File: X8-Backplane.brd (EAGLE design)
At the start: 122.1 x 106.6 mm, 18 parts, among them U1 BD6221FSOP, U2 MIC29501-5.0WU, U3 MIC29501-5.0WU, U4 FQB27P06, U5 FQB27P06, U6 FQB27P06

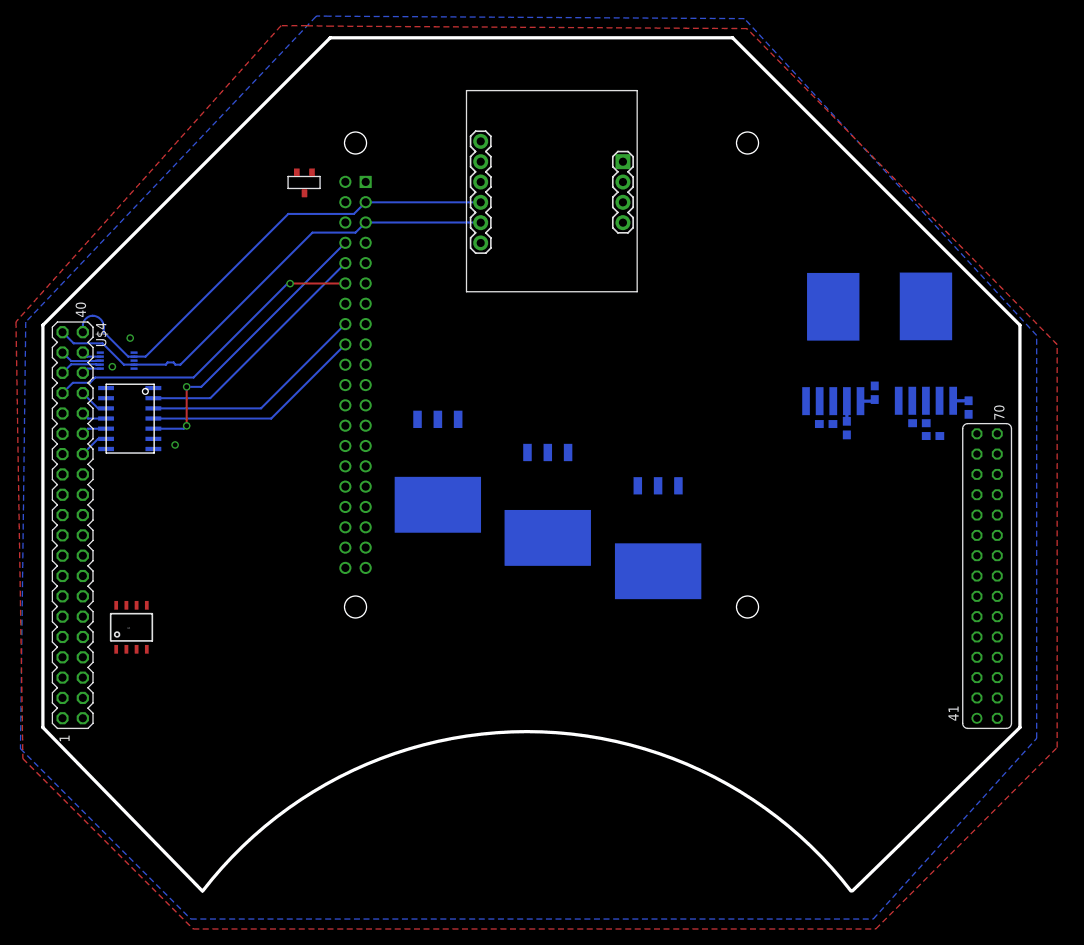
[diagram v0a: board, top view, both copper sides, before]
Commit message: Almost done with routing - stil have to add vias and extra debugging pinouts
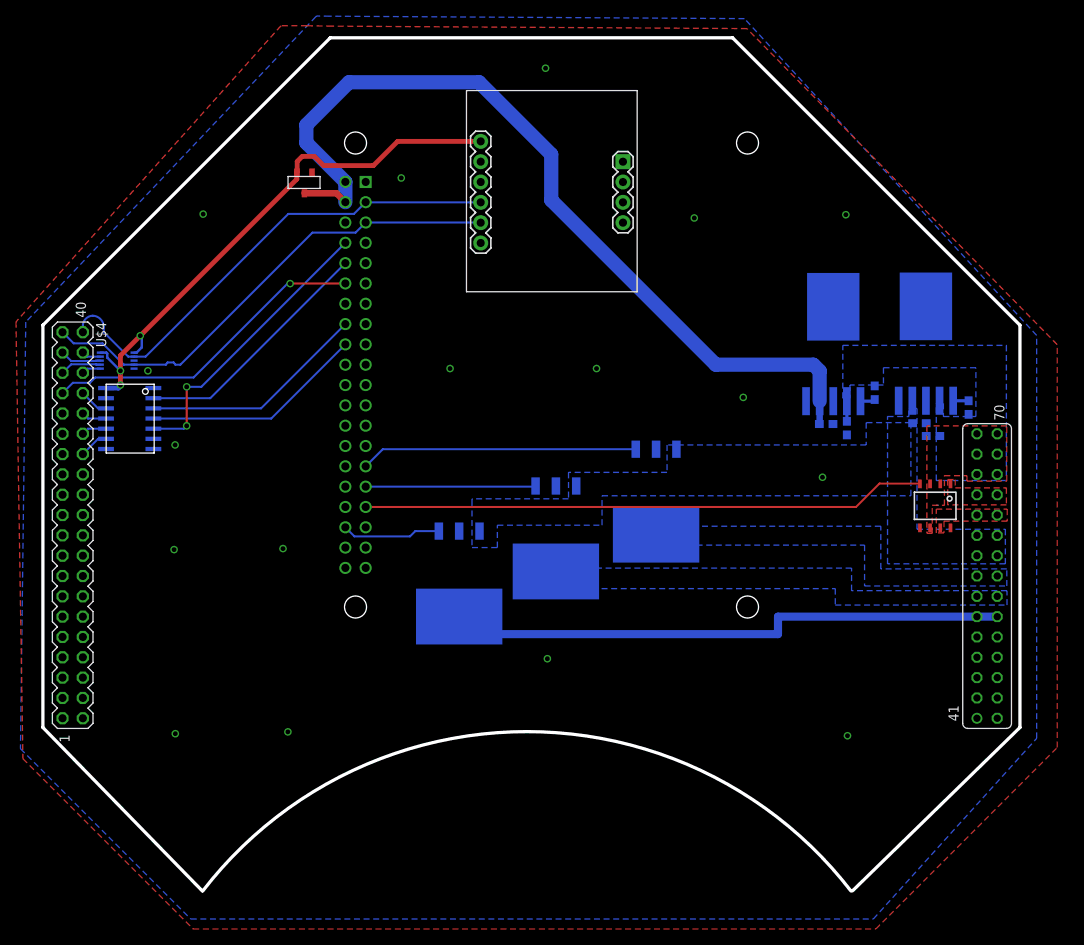
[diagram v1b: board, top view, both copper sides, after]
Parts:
- moved U1 107.3 mm to (116.4, 43.0), turned to 180 degrees
- moved U6 14.2 mm to (54.4, 32.5)
- moved U5 4.58 mm to (79.0, 42.8)
- moved U4 4.31 mm to (66.5, 38.2)
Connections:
- removed net BT_LED_5V: U$4.15, U$4.16, U6.TAB
- new net +5V_BT_LED: U$4.51, U$4.52, U6.TAB
- net +12V: now also U$4.65; no longer U$4.63, U$4.64
- net +5V_CAMERA_TUBE: now also U$4.57, U$4.58, U$4.59, U$4.60; no longer U$4.53, U$4.54, U$4.55, U$4.56
- net +5V_LASER: now also U$4.55, U$4.56; no longer U$4.59, U$4.60
- net +5V_LED: now also U$4.53, U$4.54; no longer U$4.57, U$4.58
- net 3V3_PIEZO: now also U$4.63, U$4.64; no longer U$4.10, U$4.9
- net GND_PIEZO: now also U$4.61, U$4.62; no longer U$4.11, U$4.12
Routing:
- net +5V: track 0.00 -> 108.6 mm
- net 3.3V: track 0.00 -> 71.9 mm, vias 0 -> 3
- net +5V_BT_LED: track 0.00 -> 71.6 mm
- net FIN: track 0.00 -> 70.5 mm
- net LASER_ON: track 0.00 -> 34.6 mm
- net LED_ON: track 0.00 -> 21.3 mm
- net BT_LED_ON: track 0.00 -> 12.4 mm
- added copper zone on layer 1, net +12V
- added copper zone on layer 16, net +12V
- added copper zone on layer 16, net +5V_CAMERA_TUBE
- added copper zone on layer 16, net +5V_LASER
- added copper zone on layer 16, net +5V_LED
- added copper zone on layer 1, net 3V3_PIEZO
- added copper zone on layer 1, net GND_PIEZO

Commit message: Finished routing except for any debug pins and possible extra vias
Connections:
- net GND: now also U$4.1, U$4.2, U$4.3, U$4.4
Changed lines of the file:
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@@
 <via x="18.8976" y="48.387" extent="1-16" drill="0.6"/>
 <via x="15.494" y="57.658" extent="1-16" drill="0.6"/>
+<contactref element="U$4" pad="4"/>
+<contactref element="U$4" pad="2"/>
+<contactref element="U$4" pad="1"/>
+<contactref element="U$4" pad="3"/>
+<wire x1="101.1682" y1="65.659" x2="112.7506" y2="65.7098" width="0" layer="19" extent="16-16"/>
+<wire x1="112.7506" y1="53.9115" x2="112.7506" y2="65.7098" width="0" layer="19" extent="16-16"/>
+<wire x1="112.7878" y1="51.1048" x2="112.7506" y2="53.9115" width="0" layer="19" extent="16-16"/>
+<wire x1="112.7896" y1="49.5046" x2="112.7878" y2="51.1048" width="0" layer="19" extent="16-16"/>
+<wire x1="102.87" y1="49.6452" x2="112.7896" y2="49.5046" width="0" layer="19" extent="16-16"/>
+<wire x1="101.1292" y1="51.0032" x2="102.87" y2="49.6452" width="0" layer="19" extent="16-16"/>
+<wire x1="101.1682" y1="53.8607" x2="101.1292" y2="51.0032" width="0" layer="19" extent="16-16"/>
+<wire x1="115.8132" y1="38.0268" x2="112.7896" y2="49.5046" width="0" layer="19" extent="1-16"/>
+<wire x1="119.126" y1="24.384" x2="115.8132" y2="38.0268" width="0" layer="19" extent="1-1"/>
+<wire x1="121.666" y1="24.384" x2="119.126" y2="24.384" width="0" layer="19" extent="1-1"/>
+<wire x1="121.666" y1="21.844" x2="121.666" y2="24.384" width="0" layer="19" extent="1-1"/>
+<wire x1="119.126" y1="21.844" x2="119.126" y2="24.384" width="0" layer="19" extent="1-1"/>
+<wire x1="121.666" y1="19.304" x2="121.666" y2="21.844" width="0" layer="19" extent="1-1"/>
+<wire x1="119.126" y1="19.304" x2="119.126" y2="21.844" width="0" layer="19" extent="1-1"/>
+<wire x1="121.666" y1="16.764" x2="121.666" y2="19.304" width="0" layer="19" extent="1-1"/>
+<wire x1="119.126" y1="16.764" x2="119.126" y2="19.304" width="0" layer="19" extent="1-1"/>
+<wire x1="121.666" y1="14.224" x2="121.666" y2="16.764" width="0" layer="19" extent="1-1"/>
+<wire x1="119.126" y1="14.224" x2="119.126" y2="16.764" width="0" layer="19" extent="1-1"/>
+<wire x1="57.0992" y1="81.2546" x2="101.1682" y2="65.659" width="0" layer="19" extent="16-16"/>
+<wire x1="42.718" y1="71.115" x2="57.0992" y2="81.2546" width="0" layer="19" extent="1-1"/>
+<wire x1="40.178" y1="76.195" x2="42.718" y2="71.115" width="0" layer="19" extent="1-1"/>
+<wire x1="40.178" y1="66.035" x2="42.718" y2="71.115" width="0" layer="19" extent="1-1"/>
+<wire x1="36.0172" y1="82.4484" x2="40.178" y2="76.195" width="0" layer="19" extent="1-1"/>
+<wire x1="40.178" y1="58.415" x2="40.178" y2="66.035" width="0" layer="19" extent="1-1"/>
+<wire x1="42.718" y1="50.795" x2="40.178" y2="58.415" width="0" layer="19" extent="1-1"/>
+<wire x1="40.178" y1="45.715" x2="42.718" y2="50.795" width="0" layer="19" extent="1-1"/>
+<wire x1="40.178" y1="40.635" x2="40.178" y2="45.715" width="0" layer="19" extent="1-1"/>
+<wire x1="42.718" y1="33.015" x2="40.178" y2="40.635" width="0" layer="19" extent="1-1"/>
+<wire x1="18.8976" y1="48.387" x2="40.178" y2="45.715" width="0" layer="19" extent="1-1"/>
+<wire x1="16.1798" y1="47.879" x2="18.8976" y2="48.387" width="0" layer="19" extent="16-16"/>
+<wire x1="16.1798" y1="49.149" x2="16.1798" y2="47.879" width="0" layer="19" extent="16-16"/>
+<wire x1="15.494" y1="57.658" x2="16.1798" y2="49.149" width="0" layer="19" extent="16-16"/>
+<wire x1="13.7681" y1="57.928" x2="15.494" y2="57.658" width="0" layer="19" extent="16-16"/>
+<wire x1="7.366" y1="16.764" x2="16.1798" y2="47.879" width="0" layer="19" extent="16-16"/>
+<wire x1="7.366" y1="14.224" x2="7.366" y2="16.764" width="0" layer="19" extent="1-1"/>
+<wire x1="4.826" y1="16.764" x2="7.366" y2="16.764" width="0" layer="19" extent="1-1"/>
+<wire x1="4.826" y1="14.224" x2="7.366" y2="14.224" width="0" layer="19" extent="1-1"/>
 </signal>
 <signal name="+12V">

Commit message: minor changes by Ryan
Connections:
- net A renamed TX_H
- net B renamed TX_L
- net Y renamed RX_L
- net Z renamed RX_H
- net 3.3V: now also U$4.25, U$4.26
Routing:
- net 3.3V: track 71.9 -> 87.5 mm
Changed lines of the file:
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@@
 <contactref element="U$4" pad="1"/>
 <contactref element="U$4" pad="3"/>
-<wire x1="101.1682" y1="65.659" x2="112.7506" y2="65.7098" width="0" layer="19" extent="16-16"/>
-<wire x1="112.7506" y1="53.9115" x2="112.7506" y2="65.7098" width="0" layer="19" extent="16-16"/>
-<wire x1="112.7878" y1="51.1048" x2="112.7506" y2="53.9115" width="0" layer="19" extent="16-16"/>
-<wire x1="112.7896" y1="49.5046" x2="112.7878" y2="51.1048" width="0" layer="19" extent="16-16"/>
-<wire x1="102.87" y1="49.6452" x2="112.7896" y2="49.5046" width="0" layer="19" extent="16-16"/>
-<wire x1="101.1292" y1="51.0032" x2="102.87" y2="49.6452" width="0" layer="19" extent="16-16"/>
-<wire x1="101.1682" y1="53.8607" x2="101.1292" y2="51.0032" width="0" layer="19" extent="16-16"/>
-<wire x1="115.8132" y1="38.0268" x2="112.7896" y2="49.5046" width="0" layer="19" extent="1-16"/>
-<wire x1="119.126" y1="24.384" x2="115.8132" y2="38.0268" width="0" layer="19" extent="1-1"/>
-<wire x1="121.666" y1="24.384" x2="119.126" y2="24.384" width="0" layer="19" extent="1-1"/>
-<wire x1="121.666" y1="21.844" x2="121.666" y2="24.384" width="0" layer="19" extent="1-1"/>
-<wire x1="119.126" y1="21.844" x2="119.126" y2="24.384" width="0" layer="19" extent="1-1"/>
-<wire x1="121.666" y1="19.304" x2="121.666" y2="21.844" width="0" layer="19" extent="1-1"/>
-<wire x1="119.126" y1="19.304" x2="119.126" y2="21.844" width="0" layer="19" extent="1-1"/>
-<wire x1="121.666" y1="16.764" x2="121.666" y2="19.304" width="0" layer="19" extent="1-1"/>
-<wire x1="119.126" y1="16.764" x2="119.126" y2="19.304" width="0" layer="19" extent="1-1"/>
-<wire x1="121.666" y1="14.224" x2="121.666" y2="16.764" width="0" layer="19" extent="1-1"/>
-<wire x1="119.126" y1="14.224" x2="119.126" y2="16.764" width="0" layer="19" extent="1-1"/>
-<wire x1="57.0992" y1="81.2546" x2="101.1682" y2="65.659" width="0" layer="19" extent="16-16"/>
-<wire x1="42.718" y1="71.115" x2="57.0992" y2="81.2546" width="0" layer="19" extent="1-1"/>
-<wire x1="40.178" y1="76.195" x2="42.718" y2="71.115" width="0" layer="19" extent="1-1"/>
-<wire x1="40.178" y1="66.035" x2="42.718" y2="71.115" width="0" layer="19" extent="1-1"/>
-<wire x1="36.0172" y1="82.4484" x2="40.178" y2="76.195" width="0" layer="19" extent="1-1"/>
-<wire x1="40.178" y1="58.415" x2="40.178" y2="66.035" width="0" layer="19" extent="1-1"/>
-<wire x1="42.718" y1="50.795" x2="40.178" y2="58.415" width="0" layer="19" extent="1-1"/>
-<wire x1="40.178" y1="45.715" x2="42.718" y2="50.795" width="0" layer="19" extent="1-1"/>
-<wire x1="40.178" y1="40.635" x2="40.178" y2="45.715" width="0" layer="19" extent="1-1"/>
-<wire x1="42.718" y1="33.015" x2="40.178" y2="40.635" width="0" layer="19" extent="1-1"/>
-<wire x1="18.8976" y1="48.387" x2="40.178" y2="45.715" width="0" layer="19" extent="1-1"/>
-<wire x1="16.1798" y1="47.879" x2="18.8976" y2="48.387" width="0" layer="19" extent="16-16"/>
-<wire x1="16.1798" y1="49.149" x2="16.1798" y2="47.879" width="0" layer="19" extent="16-16"/>
-<wire x1="15.494" y1="57.658" x2="16.1798" y2="49.149" width="0" layer="19" extent="16-16"/>
-<wire x1="13.7681" y1="57.928" x2="15.494" y2="57.658" width="0" layer="19" extent="16-16"/>
-<wire x1="7.366" y1="16.764" x2="16.1798" y2="47.879" width="0" layer="19" extent="16-16"/>
-<wire x1="7.366" y1="14.224" x2="7.366" y2="16.764" width="0" layer="19" extent="1-1"/>
-<wire x1="4.826" y1="16.764" x2="7.366" y2="16.764" width="0" layer="19" extent="1-1"/>
-<wire x1="4.826" y1="14.224" x2="7.366" y2="14.224" width="0" layer="19" extent="1-1"/>
 </signal>
 <signal name="+12V">
@@
 <wire x1="14.732" y1="61.849" x2="14.5415" y2="62.0395" width="0.3048" layer="16"/>
 <via x="14.5415" y="62.0395" extent="1-16" drill="0.6" diameter="0.3048"/>
-<wire x1="12.065" y1="59.563" x2="12.065" y2="57.785" width="0.6096" layer="1"/>
+<wire x1="12.065" y1="59.563" x2="12.065" y2="57.658" width="0.6096" layer="1"/>
 <via x="12.065" y="55.88" extent="1-16" drill="0.6" diameter="0.3048"/>
-<wire x1="12.065" y1="57.785" x2="12.065" y2="57.658" width="0.6096" layer="1"/>
 <wire x1="12.065" y1="57.658" x2="12.065" y2="55.88" width="0.6096" layer="1"/>
 <wire x1="12.065" y1="55.88" x2="12.065" y2="55.753" width="0.6096" layer="16"/>
@@
 <wire x1="10.414" y1="59.309" x2="12.065" y2="57.658" width="0.3048" layer="16"/>
 <via x="12.065" y="57.658" extent="1-16" drill="0.6" diameter="0.3048"/>
+<contactref element="U$4" pad="25"/>
+<contactref element="U$4" pad="26"/>
+<wire x1="4.826" y1="44.704" x2="7.366" y2="44.704" width="0.6096" layer="1"/>
+<wire x1="7.366" y1="44.704" x2="12.065" y2="49.403" width="0.6096" layer="1"/>
+<wire x1="12.065" y1="49.403" x2="12.065" y2="55.88" width="0.6096" layer="1"/>
 </signal>
 <signal name="SDA">
@@
 <wire x1="23.292" y1="54.229" x2="40.178" y2="71.115" width="0.254" layer="16"/>
 </signal>
-<signal name="A">
+<signal name="TX_H">
 <contactref element="U$1" pad="A"/>
 <contactref element="U$4" pad="34"/>
@@
 <wire x1="9.271" y1="52.959" x2="7.366" y2="54.864" width="0.254" layer="16"/>
 </signal>
-<signal name="B">
+<signal name="TX_L">
 <contactref element="U$1" pad="B"/>
 <contactref element="U$4" pad="32"/>
 <wire x1="10.2613" y1="51.689" x2="8.001" y2="51.689" width="0.254" layer="16"/>
 <wire x1="8.001" y1="51.689" x2="7.366" y2="52.324" width="0.254" layer="16"/>
-</signal>
-<signal name="Z">
-<contactref element="U$1" pad="Z"/>
-<contactref element="U$4" pad="30"/>
-<wire x1="10.2613" y1="50.419" x2="8.001" y2="50.419" width="0.254" layer="16"/>
-<wire x1="8.001" y1="50.419" x2="7.366" y2="49.784" width="0.254" layer="16"/>
-</signal>
-<signal name="Y">
-<contactref element="U$1" pad="Y"/>
-<contactref element="U$4" pad="28"/>
-<wire x1="10.2613" y1="49.149" x2="9.271" y2="49.149" width="0.254" layer="16"/>
-<wire x1="9.271" y1="49.149" x2="7.366" y2="47.244" width="0.254" layer="16"/>
 </signal>
 <signal name="TX">
@@
 <via x="65.4304" y="21.6662" extent="1-16" drill="0.6" diameter="0.3048"/>
 </signal>
+<signal name="RX_H">
+<contactref element="U$1" pad="Z"/>
+<contactref element="U$4" pad="30"/>
+<wire x1="8.001" y1="50.419" x2="7.366" y2="49.784" width="0.254" layer="16"/>
+<wire x1="8.001" y1="50.419" x2="10.2613" y2="50.419" width="0.254" layer="16"/>
+</signal>
+<signal name="RX_L">
+<contactref element="U$1" pad="Y"/>
+<contactref element="U$4" pad="28"/>
+<wire x1="9.271" y1="49.149" x2="7.366" y2="47.244" width="0.254" layer="16"/>
+<wire x1="9.271" y1="49.149" x2="10.2613" y2="49.149" width="0.254" layer="16"/>
+</signal>
 </signals>

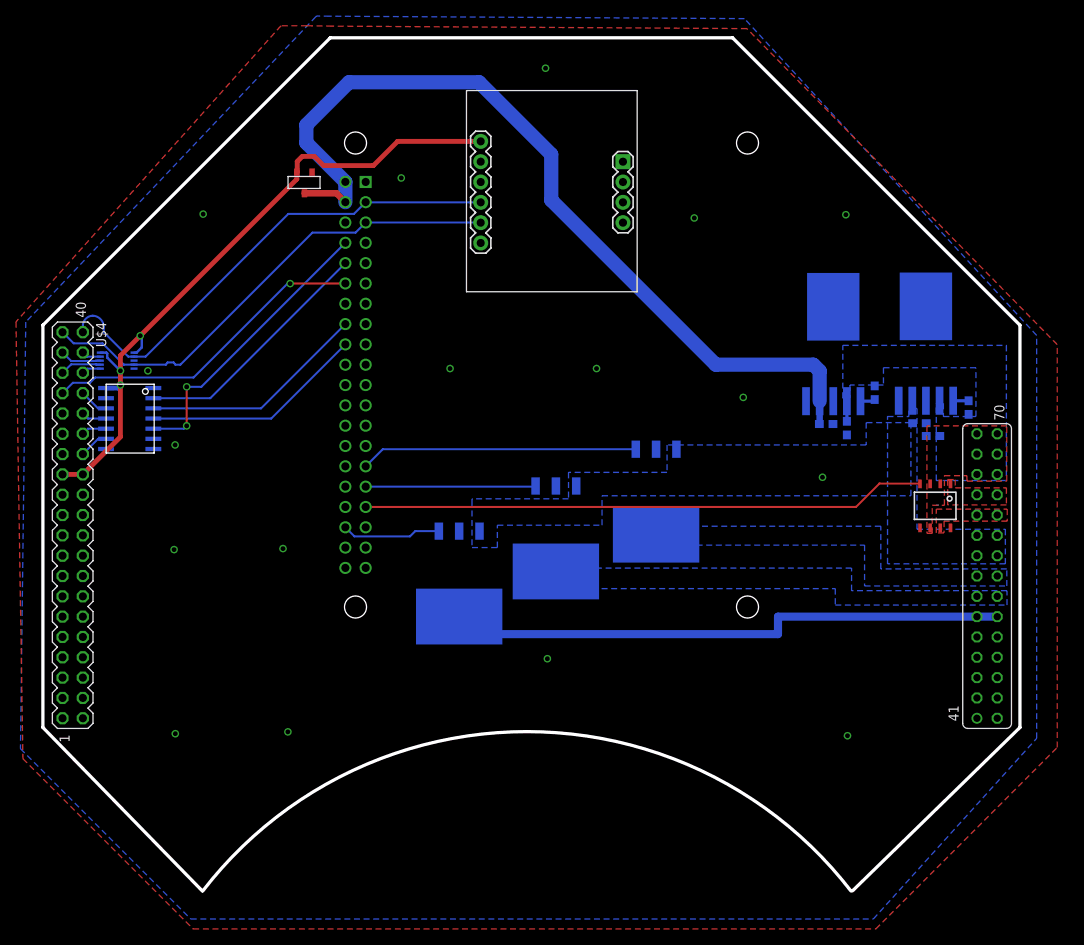
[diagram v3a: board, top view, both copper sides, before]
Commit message: made the bottom flat
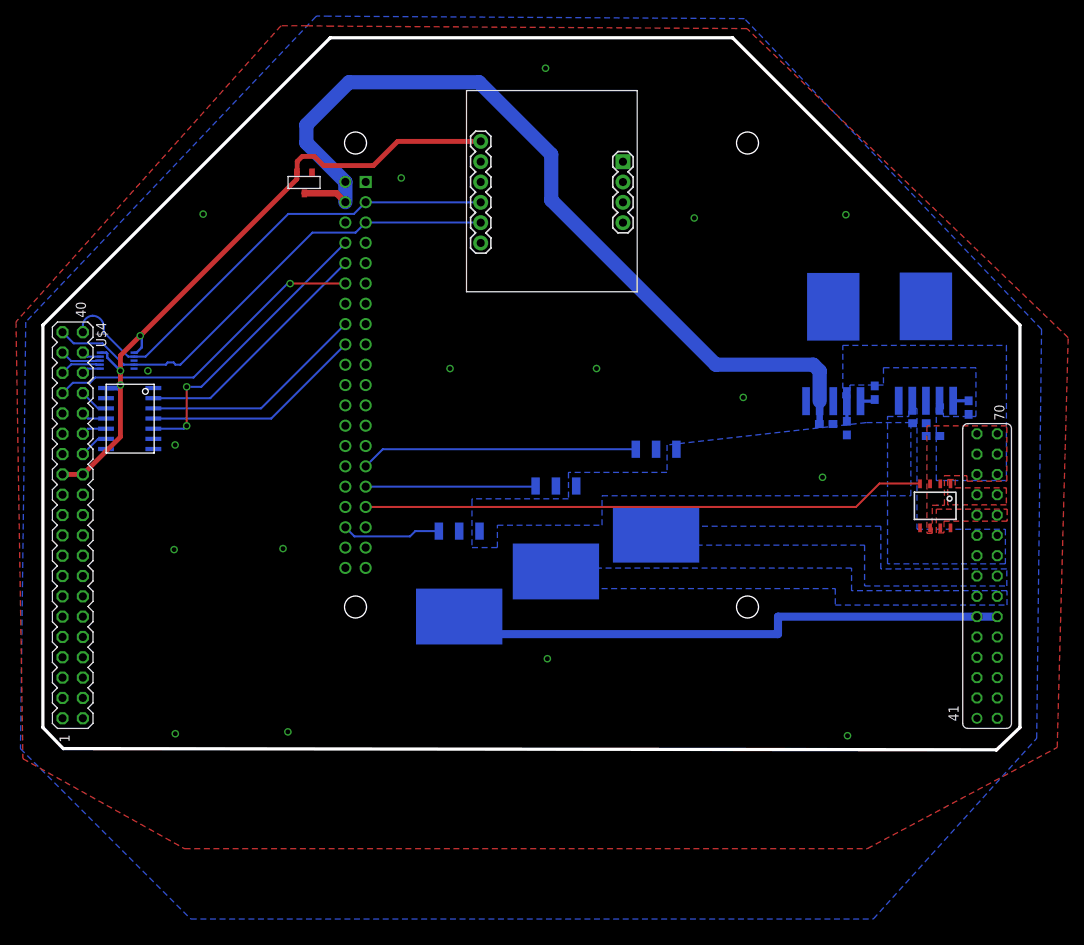
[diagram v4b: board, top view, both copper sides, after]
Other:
- board size 122.1 x 106.6 mm -> 122.1 x 89 mm
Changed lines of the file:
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@@
 <circle x="63.43686875" y="38.21558125" radius="73.025" width="0.4064" layer="51"/>
 <wire x1="38.29215" y1="99.28131875" x2="2.371125" y2="63.36029375" width="0.4064" layer="20"/>
-<wire x1="124.50260625" y1="13.0708625" x2="103.567584375" y2="-7.3561625" width="0.4064" layer="20"/>
-<wire x1="2.371125" y1="13.0708625" x2="22.29015" y2="-7.3561625" width="0.4064" layer="20"/>
+<wire x1="124.50260625" y1="13.0708625" x2="121.550784375" y2="10.2460375" width="0.4064" layer="20"/>
+<wire x1="2.371125" y1="13.0708625" x2="4.91655" y2="10.4238375" width="0.4064" layer="20"/>
 <wire x1="88.581584375" y1="99.28131875" x2="124.50260625" y2="63.36029375" width="0.4064" layer="20"/>
 <wire x1="88.581584375" y1="99.28131875" x2="38.29215" y2="99.28131875" width="0.4064" layer="20"/>
 <wire x1="124.50260625" y1="63.36029375" x2="124.50260625" y2="13.0708625" width="0.4064" layer="20"/>
 <wire x1="2.371125" y1="63.36029375" x2="2.371125" y2="13.0708625" width="0.4064" layer="20"/>
-<wire x1="22.352" y1="-7.366" x2="103.378" y2="-7.366" width="0.4064" layer="20" curve="-104.736525"/>
+<wire x1="121.576184375" y1="10.27971875" x2="4.94195" y2="10.43211875" width="0.4064" layer="20"/>
 </plain>
 <attributes>
@@
 <vertex x="106.172" y="-10.8712"/>
 <vertex x="126.5936" y="11.7094"/>
-<vertex x="126.5936" y="62.0776"/>
+<vertex x="127.2032" y="62.8396"/>
 <vertex x="90.0684" y="101.6762"/>
 <vertex x="38.227" y="101.981"/>
@@
 <vertex x="-0.9906" y="63.7794"/>
 <vertex x="-0.127" y="9.1694"/>
-<vertex x="21.1582" y="-12.1158"/>
-<vertex x="106.4768" y="-12.1158"/>
+<vertex x="20.0914" y="-2.0828"/>
+<vertex x="105.41" y="-2.0828"/>
 <vertex x="129.159" y="10.5664"/>
-<vertex x="129.159" y="60.9346"/>
+<vertex x="130.5306" y="61.7982"/>
 <vertex x="90.3732" y="100.4316"/>
 <vertex x="38.5318" y="100.7364"/>
@@
 <vertex x="110.871" y="51.181"/>
 <vertex x="105.283" y="51.181"/>
-<vertex x="105.283" y="48.387"/>
 <vertex x="80.391" y="48.387"/>
 <vertex x="80.391" y="44.958"/>
